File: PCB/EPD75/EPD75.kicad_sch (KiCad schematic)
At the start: 120 parts, among them J1 Conn_01x26, J2 Shelly, J3 USB-PROG, J4 BTN1, J5 USB-C-Socket-V, J6 BTN2, J7 USB-C-Socket-V, J8 PWR, J9 PWR, P41 -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

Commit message: Caps, etc.
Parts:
- added C28: C_Polarized, Capacitor_Tantalum_SMD:CP_EIA-7343-31_Kemet-D, symbol Device:C_Polarized
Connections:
- net GND: now also C28.2
- net VBUS: now also C28.1
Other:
- moved on the sheet: J5, J7, R2, R3

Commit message: Res
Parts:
- R1: value 0.47R -> 0.22R
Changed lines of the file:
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@@
       (effects (font (size 1.27 1.27)))
     )
-    (property "Value" "0.47R" (at 183.515 157.48 90)
+    (property "Value" "0.22R" (at 183.515 157.48 90)
       (effects (font (size 1.27 1.27)))
     )

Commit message: more caps, etc
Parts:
- removed D4: BAV99S, RevK:SOT-363_SC-70-6, symbol Diode:BAV99S
- added C28: 22uF 35V, RevK:C_1210, symbol Device:C
- added D4, D7: ~, RevK:DFN1006-2L, symbol RevK:ES05D1MC10
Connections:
- net GND: now also C28.2, D4.1, D7.1
- net PWR: now also C28.1
- net at J6.2 (Pin_2), P43.1 (P), R12.1: now also D4.2
- net at J4.2 (Pin_2), P44.1 (P), R13.1: now also D7.2
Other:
- moved on the sheet: C7, C8, J4, J6, R12, R13

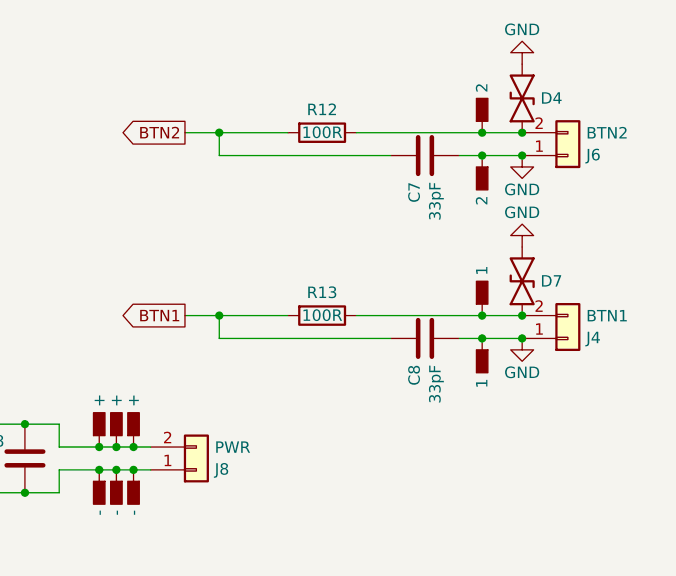
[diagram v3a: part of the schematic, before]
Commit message: More ESD
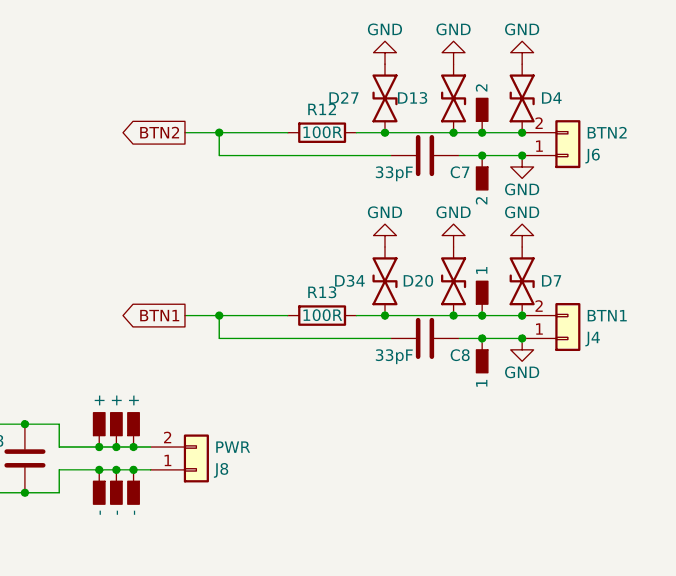
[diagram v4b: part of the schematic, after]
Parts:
- added D13, D20, D27, D34: ~, RevK:DFN1006-2L, symbol RevK:ES05D1MC10
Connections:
- net GND: now also D13.1, D20.1, D27.1, D34.1
- net at D4.2, J6.2 (Pin_2), P43.1 (P)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: now also D13.2, D27.2
- net at D7.2, J4.2 (Pin_2), P44.1 (P)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: now also D20.2, D34.2

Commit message: Reverse tantilum
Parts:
- C28: JLCPCB Rotation Offset (none) -> 180
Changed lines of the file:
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@@
+      (effects (font (size 1.27 1.27)) hide)
+    )
+    (property "JLCPCB Rotation Offset" "180" (at 245.745 100.33 0)
       (effects (font (size 1.27 1.27)) hide)
     )

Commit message: SS
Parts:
- C28: footprint Capacitor_Tantalum_SMD:CP_EIA-7343-31_Kemet-D -> RevK:CP_EIA-7343-31_Kemet-D
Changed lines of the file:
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@@
       (effects (font (size 1.27 1.27)) (justify right))
     )
-    (property "Footprint" "Capacitor_Tantalum_SMD:CP_EIA-7343-31_Kemet-D" (at 244.7798 96.52 0)
+    (property "Footprint" "RevK:CP_EIA-7343-31_Kemet-D" (at 244.7798 96.52 0)
       (effects (font (size 1.27 1.27)) hide)
     )

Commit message: Tweak
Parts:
- added P42: -, RevK:SolderPad, symbol RevK:SolderPad
- added P46: +, RevK:SolderPad, symbol RevK:SolderPad
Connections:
- net GND: now also P42.1 (P)
- net PWR: now also P46.1 (P)
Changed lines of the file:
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@@
   (junction (at 259.715 48.895) (diameter 0) (color 0 0 0 0)
   )
+  (junction (at 218.44 63.5) (diameter 0) (color 0 0 0 0)
+  )
   (junction (at 37.465 128.27) (diameter 0) (color 0 0 0 0)
   )
@@
   )
   (junction (at 267.335 28.575) (diameter 0) (color 0 0 0 0)
+  )
+  (junction (at 218.44 66.04) (diameter 0) (color 0 0 0 0)
   )
   (junction (at 45.085 172.72) (diameter 0) (color 0 0 0 0)
@@
     (stroke (width 0) (type default))
   )
+  (wire (pts (xy 218.44 66.04) (xy 220.345 66.04))
+    (stroke (width 0) (type default))
+  )
   (wire (pts (xy 37.465 58.42) (xy 37.465 64.77))
     (stroke (width 0) (type default))
@@
     (stroke (width 0) (type default))
   )
+  (wire (pts (xy 218.44 63.5) (xy 220.345 63.5))
+    (stroke (width 0) (type default))
+  )
   (wire (pts (xy 37.465 96.52) (xy 37.465 102.87))
     (stroke (width 0) (type default))
@@
     (stroke (width 0) (type default))
   )
-  (wire (pts (xy 215.9 66.04) (xy 220.345 66.04))
+  (wire (pts (xy 215.9 66.04) (xy 218.44 66.04))
     (stroke (width 0) (type default))
   )
@@
     (stroke (width 0) (type default))
   )
-  (wire (pts (xy 215.9 63.5) (xy 220.345 63.5))
+  (wire (pts (xy 215.9 63.5) (xy 218.44 63.5))
     (stroke (width 0) (type default))
   )
@@
     )
   )
+  (symbol (lib_id "RevK:SolderPad") (at 218.44 66.04 270) (unit 1)
+    (in_bom no) (on_board yes) (dnp no)
+    (property "Reference" "P42" (at 218.44 72.39 0)
+      (effects (font (size 1.27 1.27)) hide)
+    )
+    (property "Value" "-" (at 218.44 70.485 0)
+      (effects (font (size 1.27 1.27)) (justify left))
+    )
+    (property "Footprint" "RevK:SolderPad" (at 215.9 66.04 0)
+      (effects (font (size 1.27 1.27)) hide)
+    )
+    (property "Datasheet" "" (at 218.44 66.04 0)
+      (effects (font (size 1.27 1.27)) hide)
+    )
+    (pin "1")
+    (instances
+      (project "GenericS3"
+        (path "/2d210a96-f81f-42a9-8bf4-1b43c11086f3"
+          (reference "P42") (unit 1)
+        )
+      )
+      (project "EPD75"
+        (path "/46c350bb-7de4-4e81-aafd-4af55e37aab0"
+          (reference "P18") (unit 1)
+        )
+      )
+    )
+  )
   (symbol (lib_id "power:+3.3V") (at 27.94 35.56 0) (unit 1)
     (in_bom yes) (on_board yes) (dnp no)
@@
         )
       )
+    )
+  )
+  (symbol (lib_id "RevK:SolderPad") (at 218.44 63.5 90) (unit 1)
+    (in_bom no) (on_board yes) (dnp no)
+    (property "Reference" "P46" (at 218.44 57.15 0)
+      (effects (font (size 1.27 1.27)) hide)
+    )
+    (property "Value" "+" (at 218.44 59.055 0)
+      (effects (font (size 1.27 1.27)) (justify left))
+    )
+    (property "Footprint" "RevK:SolderPad" (at 220.98 63.5 0)
+      (effects (font (size 1.27 1.27)) hide)
+    )
+    (property "Datasheet" "" (at 218.44 63.5 0)
+      (effects (font (size 1.27 1.27)) hide)
+    )
+    (pin "1")
+    (instances
+      (project "GenericS3"
+        (path "/2d210a96-f81f-42a9-8bf4-1b43c11086f3"
+          (reference "P46") (unit 1)
+        )
+      )
+      (project "EPD75"
+        (path "/46c350bb-7de4-4e81-aafd-4af55e37aab0"
+          (reference "P17") (unit 1)
+        )
+      )

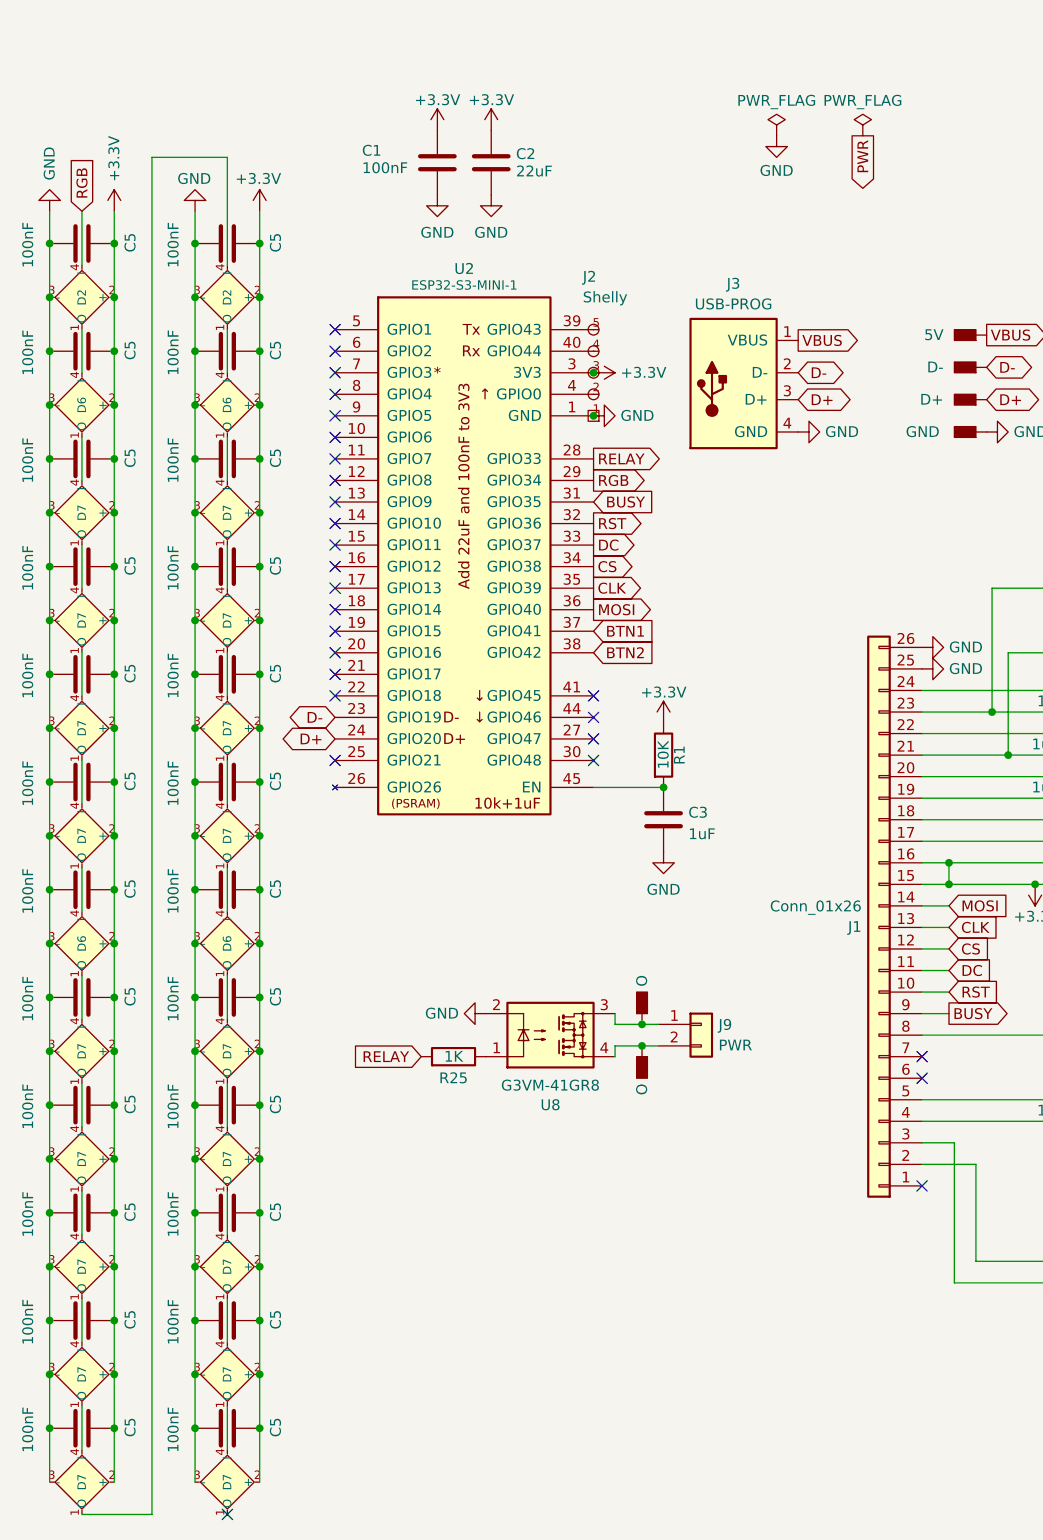
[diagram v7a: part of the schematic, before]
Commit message: Not finished adding SD slot
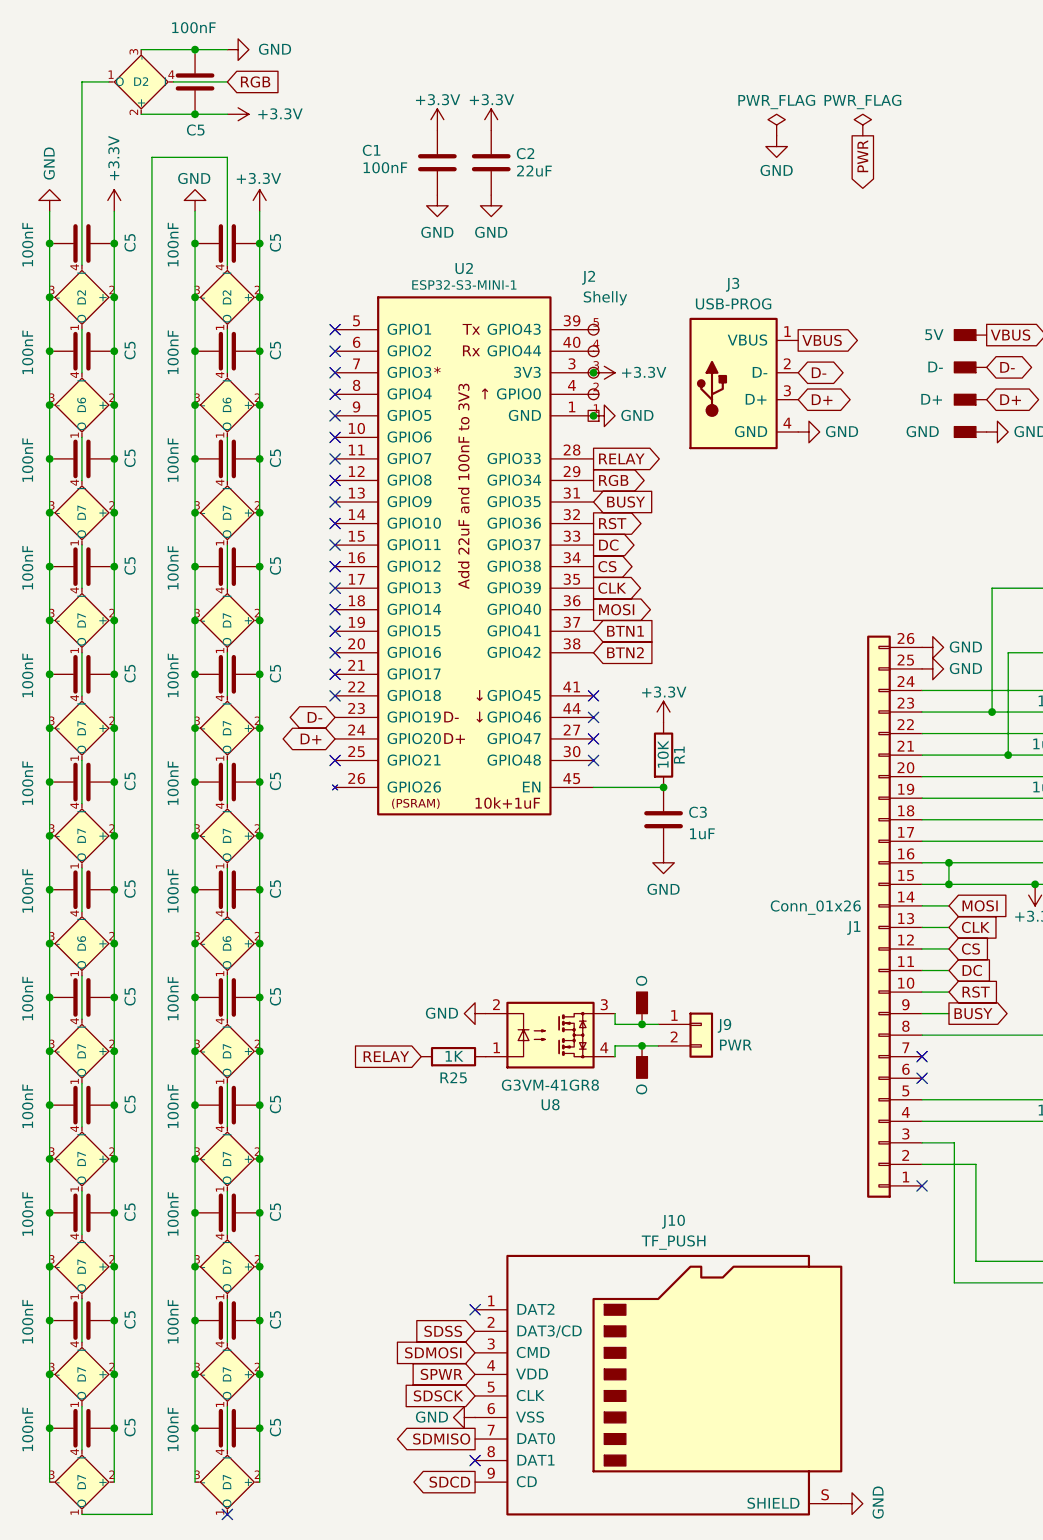
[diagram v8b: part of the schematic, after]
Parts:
- added C5: 100nF, RevK:C_0402, symbol Device:C
- added D2: XL-1010RGBC-WS2812B, RevK:SMD1010, symbol RevK:WS2812B-1mm
- added J10: TF_PUSH, RevK:TF_PUSH, symbol RevK:TF_PUSH
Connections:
- net +3.3V: now also C5.1, D2.2 (+)
- net GND: now also C5.2, D2.3 (-), J10.6 (VSS), J10.S (SHIELD)
- net RGB: now also D2.4 (I); no longer D2.4 (I)
- new net: D2.1 (O), D2.4 (I)
- new net SDCD: J10.9 (CD)
- new net SDMISO: J10.7 (DAT0)
- new net SDMOSI: J10.3 (CMD)
- new net SDSCK: J10.5 (CLK)
- new net SDSS: J10.2 (DAT3/CD)
- new net SPWR: J10.4 (VDD)
- no-connect marks 28 -> 30
